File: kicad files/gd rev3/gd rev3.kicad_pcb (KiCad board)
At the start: 4 copper layers, 286 parts, among them J1 XY, J10 Apple_II_Slot, J11 Game Port, J12 Right Angle, J13 SWD, J14 USB_A, J15 Rev2 Header, J16 RP2040 Header, J17 VGA_Micro, J18 vga_SWD, J19 SPKR, J2 DB19_4, J20 Ears, J21 KBD Serial, J22 L77HDE15SD1CH4F, J23 Game-DB VERIFY FOOTPRINT, J3 DB19_16, J4 EN, J5 DSUB19, J6 FDC Hdr, J7 EN, J8 EN, J9 IO-Xtra, Q1 BC817, Q2 BC817, Q3 BC817, Q4 BC817, Q5 BC817, Q6 BC817, Q7 BC817, Q8 BC817, Q9 BC817, SW1 MEGA RESET, SW2 DEV, SW3 IOSEL, SW4 KBD RESET, SW5 KBD Boot Sel, SW6 VGA Boot Sel, SW7 VGA RESET, U1 Apple_MEGA_II, U10 DRAM64KX4, U11 IWM, U12 Slotmaker, U13 74HCT245, U14 RP2040, U15 MIC5504-3.3YM5, U16 74HC245, U17 W25Q128JVS, U18 HCT251, U19 W25Q128JVS, U2 w65c02s, U20 NE556, U21 NE556, U22 74HCT245, U23 RP2040, U24 74LVC2G04, U26 MCP4541T, U27 LM4875, U28 SN74LVC573ANS, U29 74LVC2G04, U3 74LVC1G02, U30 74LVC2G04, U32 LM7905_TO220, U35 74LVC2G04, U4 74HCT245, U5 74HCT245, U6 AT28C256-PLCC, U7 DRAM64KX4, U8 DRAM64KX4, U9 DRAM64KX4, X1 14.31818MHz, Y1 ECS-120-18-33-JEM-TR, Y2 ECS-120-18-33-JEM-TR

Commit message: re-arranged everything... what have I done?!
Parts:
- moved J20 121.9 mm to (224.7, 86.4)
- moved R10 115.6 mm to (198.2, 98.2)
- moved U26 115.6 mm to (195.0, 94.4)
- moved C58 115.6 mm to (192.0, 94.5)
- moved C59 115.6 mm to (193.4, 88.1)
- moved C60 115.6 mm to (203.5, 83.1)
- moved D2 115.6 mm to (207.3, 98.6)
- moved J19 115.6 mm to (207.0, 88.6)
- moved R48 115.6 mm to (204.7, 98.3)
- moved R49 115.6 mm to (199.9, 92.2)
- moved R50 115.6 mm to (213.4, 92.6)
- moved R8 115.6 mm to (190.8, 88.7)
- moved R9 115.6 mm to (188.5, 88.7)
- moved U27 115.6 mm to (199.8, 87.1)
- moved C61 115.6 mm to (199.8, 83.1)
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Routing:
- net /game_port/SW1_CAPL: track 93.5 -> 0.00 mm
- net /IWM/MD7: track 420.4 -> 330.4 mm
- net /mega-6502/RGB4: track 87.4 -> 0.00 mm
- net /mega-6502/RGB1: track 86.1 -> 0.00 mm
- net /game_port/SW0_OAPL: track 84.2 -> 0.00 mm
- net /game_port/SW2: track 83.2 -> 0.00 mm
- net /mega-6502/RGB8: track 77.6 -> 0.00 mm
- net /mega-6502/RGB2: track 72.6 -> 0.00 mm
- net /IWM/MD6: track 396.3 -> 327.0 mm
- net /IWM/MD5: track 384.6 -> 316.6 mm
- net /IWM/MD4: track 393.3 -> 325.9 mm
- net /game_port/PDL3: track 66.4 -> 0.00 mm
- net /IWM/MD3: track 395.4 -> 329.2 mm
- net /IWM/MD2: track 393.2 -> 328.1 mm
- net /game_port/PDL0: track 64.9 -> 0.00 mm
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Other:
- board outline added: 165.9 x 217.3 mm

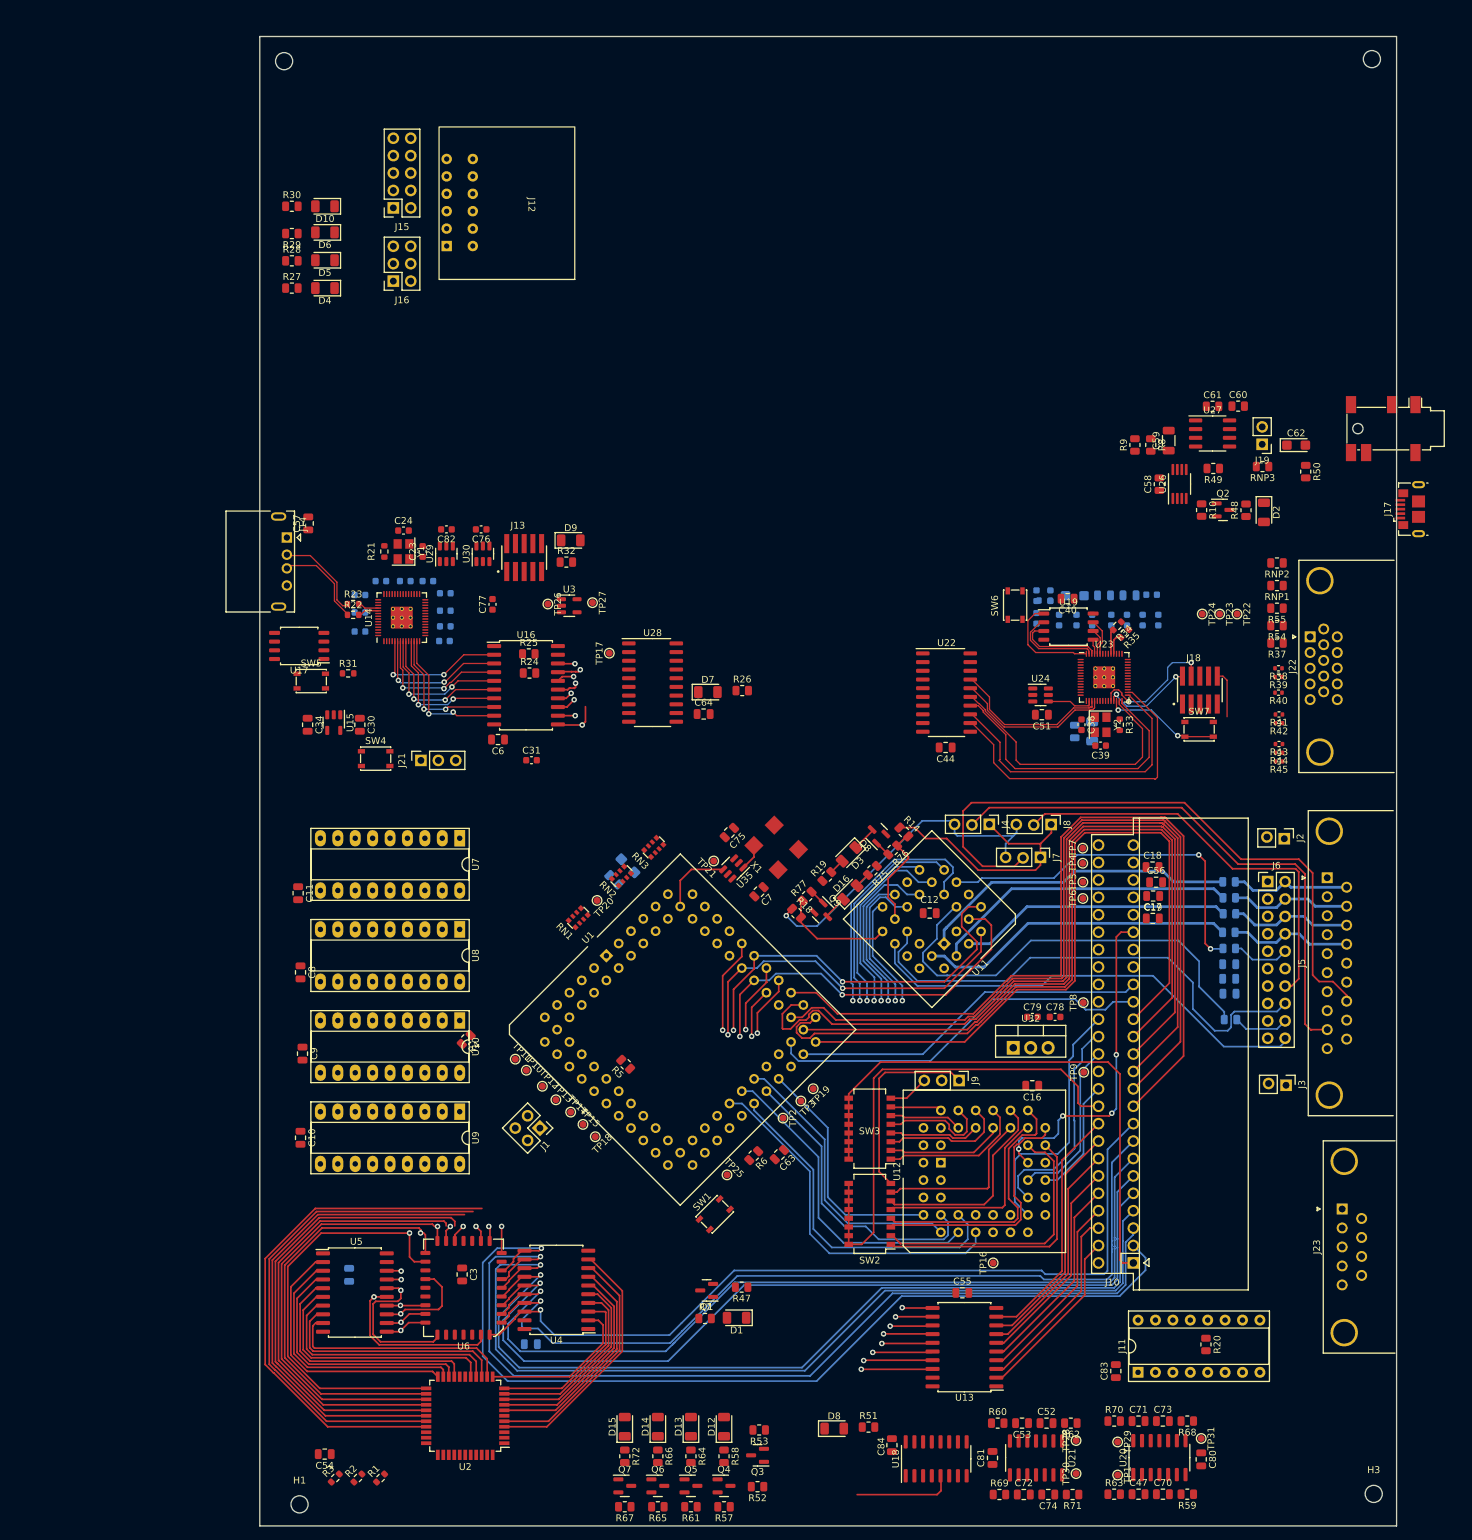
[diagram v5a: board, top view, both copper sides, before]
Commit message: moved earphone to front of board and re-arranged other groups.
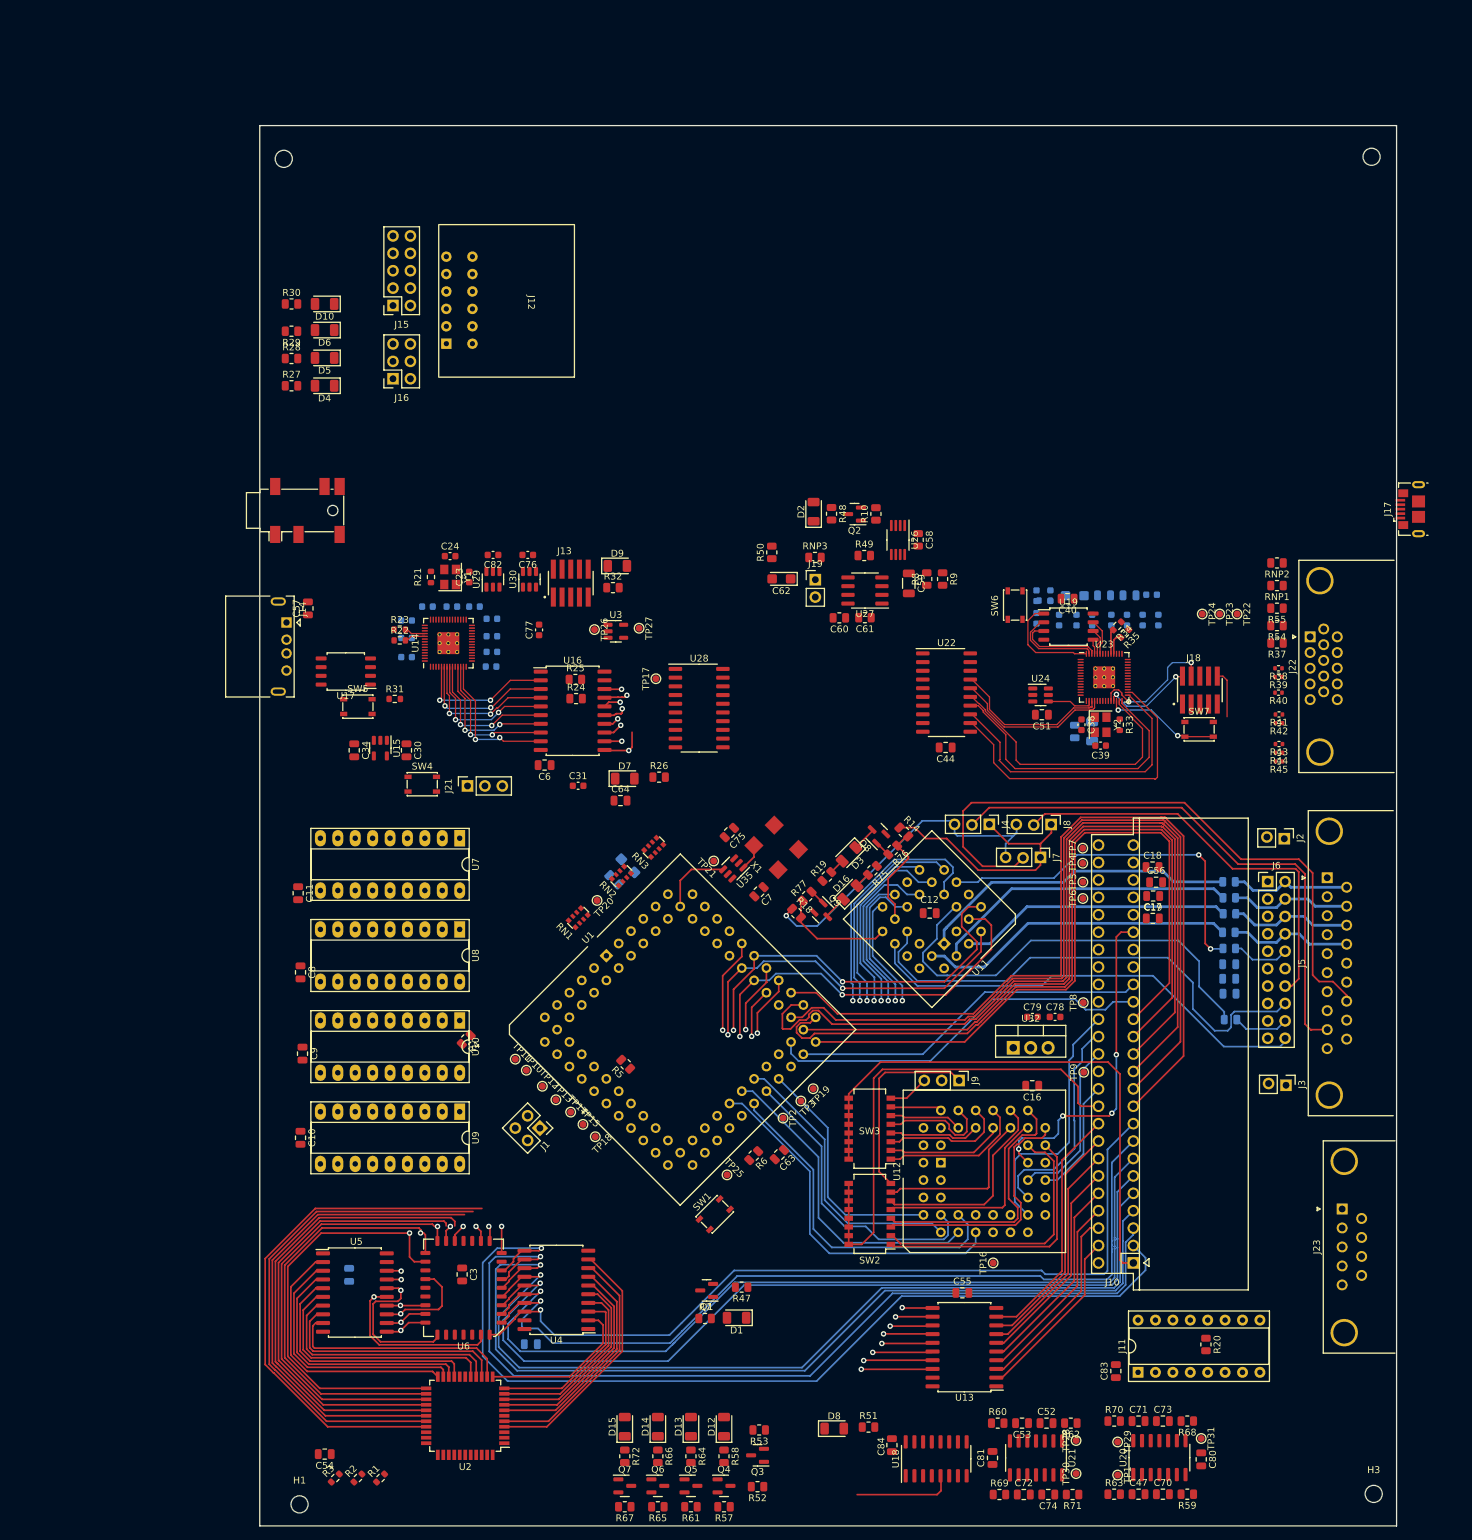
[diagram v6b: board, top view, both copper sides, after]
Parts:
- moved J20 157.4 mm to (67.8, 98.3), turned to 90 degrees
- moved R50 78.8 mm to (135.5, 104.4), turned to 90 degrees
- moved C62 77.6 mm to (136.9, 108.3), turned to 180 degrees
- moved J19 68.1 mm to (141.8, 108.4), turned to 0 degrees
- moved RNP3 66.6 mm to (141.8, 105.2), turned to 0 degrees
- moved C60 65.9 mm to (145.4, 114.0), turned to 180 degrees
- moved D2 65.7 mm to (141.6, 98.5), turned to 90 degrees
- moved R48 60.5 mm to (144.2, 98.8), turned to -90 degrees
- moved C61 59.4 mm to (149.1, 113.9), turned to 180 degrees
- moved U27 55.7 mm to (149.1, 110.0), turned to 180 degrees
- moved Q2 53.8 mm to (147.6, 98.8), turned to 180 degrees
- moved R49 52.5 mm to (149.0, 104.9), turned to 0 degrees
- moved R10 47.5 mm to (150.7, 98.8), turned to 90 degrees
- moved C59 43.3 mm to (155.5, 108.9), turned to -90 degrees
- moved U26 41.9 mm to (153.9, 102.6), turned to -90 degrees
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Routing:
- net /rp2040-keyboard/USB_D-: track 13.0 -> 0.00 mm
- net /rp2040-keyboard/USB_D+: track 12.8 -> 0.00 mm
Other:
- board size 165.9 x 217.3 mm -> 165.9 x 204.3 mm

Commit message: mdoern area clean-ups
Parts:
- moved D7 53.9 mm to (64.0, 117.3)
- moved R26 53.9 mm to (69.0, 117.1)
- moved D9 48.0 mm to (76.0, 137.0)
- moved R32 48.0 mm to (75.3, 140.2)
- moved R50 32.4 mm to (141.7, 136.2), turned to 180 degrees
- moved D2 32.2 mm to (135.7, 130.1), turned to 180 degrees
- moved R48 29.9 mm to (136.1, 127.5), turned to 0 degrees
- moved C62 27.9 mm to (145.6, 134.8), turned to -90 degrees
- moved Q2 27.8 mm to (136.1, 124.2), turned to -90 degrees
- moved R10 26.6 mm to (136.1, 121.0), turned to 180 degrees
- moved RNP3 24.8 mm to (142.4, 129.9), turned to 90 degrees
- moved J19 21.8 mm to (145.7, 129.9), turned to 90 degrees
- moved C58 21.0 mm to (139.9, 114.9), turned to 0 degrees
- moved U26 20.7 mm to (139.9, 117.8), turned to 0 degrees
- moved R38 19.1 mm to (209.7, 140.5)
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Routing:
- net Net-(J5-Pad17): track 93.3 -> 60.1 mm
- net /IWM/seek2: track 17.9 -> 1.16 mm
- net /IWM/seek0: track 17.6 -> 1.34 mm
- net /IWM/seek1: track 17.8 -> 1.76 mm
- net /IWM/seek3: track 18.0 -> 2.87 mm
- net Net-(J4-Pad2): track 79.2 -> 67.2 mm
- net Net-(J6-Pad14): track 60.9 -> 49.2 mm
- net /IWM/bWREQ: track 8.43 -> 0.85 mm
- net /IWM/MD0: track 339.4 -> 344.7 mm
- net /IWM/MD1: track 325.7 -> 330.0 mm
- net /IWM/MD2: track 328.1 -> 331.3 mm
- net /IWM/MD3: track 329.2 -> 330.7 mm
- net /IWM/SENSE: track 66.4 -> 65.3 mm
- net /IWM/MD4: track 325.9 -> 326.8 mm
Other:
- board size 165.9 x 204.3 mm -> 165.9 x 190.6 mm
